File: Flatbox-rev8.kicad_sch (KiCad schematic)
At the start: 72 parts, among them SW1 SW_Push, SW10 GPIO18, SW11 GPIO25, SW12 GPIO27, SW13 GPIO29, SW14 GPIO19, SW15 GPIO24, SW16 GPIO26, SW17 GPIO28, SW18 GPIO16, SW19 SW_Push, SW2 SW_Push, SW20 SW_Push, SW21 GPIO16, SW3 SW_Push, SW4 SW_Push, SW5 SW_Push, SW6 SW_Push, SW7 GPIO9, SW8 GPIO10, SW9 GPIO11, U1 RP2350_60QFN, U2 TLV73333PDBV, U3 W25Q128JVS, Y1 ABM8-272-T3

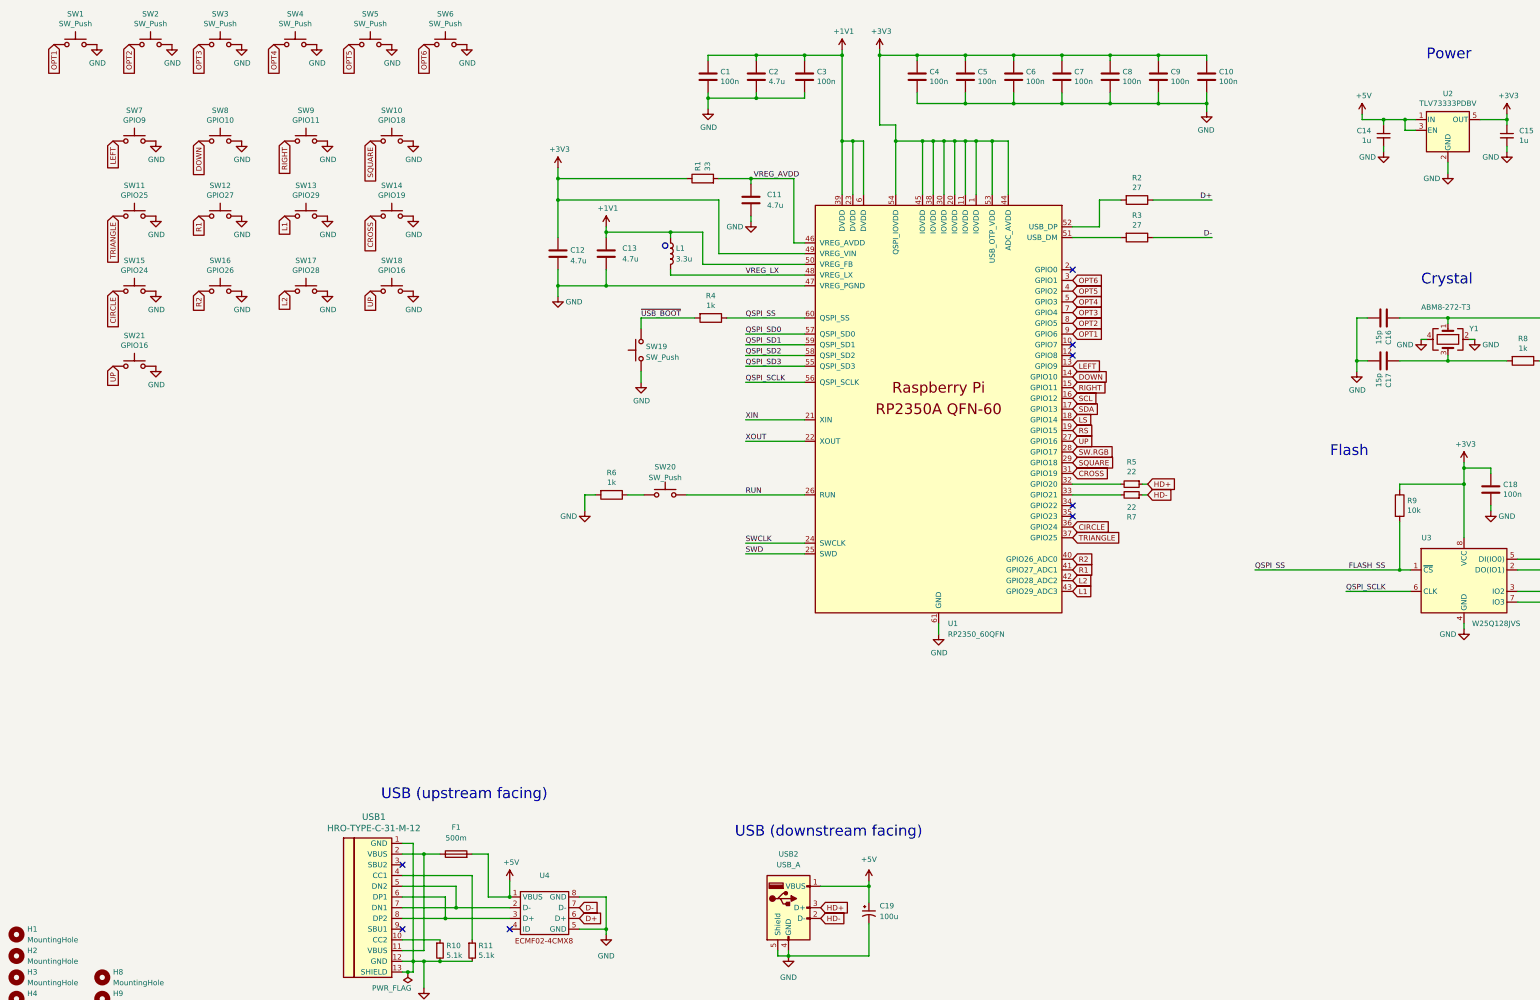
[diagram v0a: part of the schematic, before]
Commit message: Document PHBox design state and sync KiCad sources
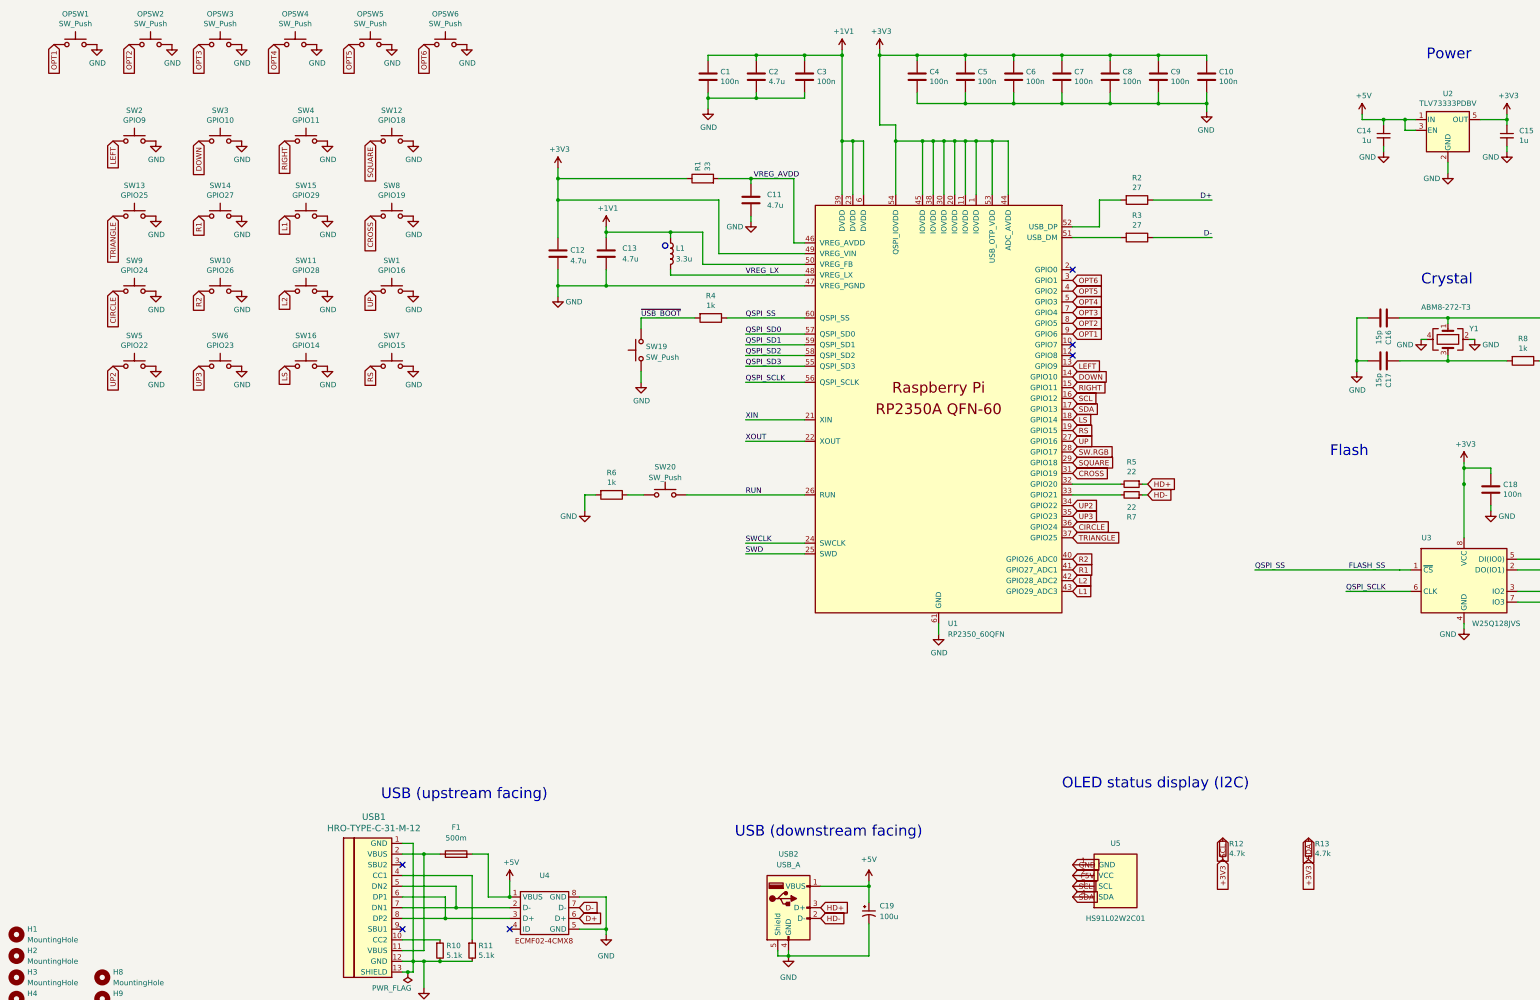
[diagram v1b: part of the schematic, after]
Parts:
- removed R9: 10k, Resistor_SMD:R_0402_1005Metric, symbol Device:R
- added R12, R13: 4.7k, PHBox:R_0603_Compact, symbol Device:R_Small
- added SW16: GPIO14, PCM_Switch_Keyboard_Hotswap_Kailh:SW_Hotswap_Kailh_Choc_V1V2, symbol Switch:SW_Push
- added SW6: GPIO23, PCM_Switch_Keyboard_Hotswap_Kailh:SW_Hotswap_Kailh_Choc_V1V2, symbol Switch:SW_Push
- added SW7: GPIO15, PCM_Switch_Keyboard_Hotswap_Kailh:SW_Hotswap_Kailh_Choc_V1V2, symbol Switch:SW_Push
- added U5: HS91L02W2C01, EasyEDA_Lib:OLED-TH_L38.0-W12.0_HS91L02W2C01, symbol PHBox:HS91L02W2C01_Module
- SW1: renamed from SW18; footprint Kailh:Kailh_socket_PG1350_optional -> PCM_Switch_Keyboard_Hotswap_Kailh:SW_Hotswap_Kailh_Choc_V1V2
- SW10: renamed from SW16; footprint Kailh:Kailh_socket_PG1350_optional -> PCM_Switch_Keyboard_Hotswap_Kailh:SW_Hotswap_Kailh_Choc_V1V2
- SW11: renamed from SW17; footprint Kailh:Kailh_socket_PG1350_optional -> PCM_Switch_Keyboard_Hotswap_Kailh:SW_Hotswap_Kailh_Choc_V1V2
- SW12: renamed from SW10; footprint Kailh:Kailh_socket_PG1350_optional -> PCM_Switch_Keyboard_Hotswap_Kailh:SW_Hotswap_Kailh_Choc_V1V2
- SW13: renamed from SW11; footprint Kailh:Kailh_socket_PG1350_optional -> PCM_Switch_Keyboard_Hotswap_Kailh:SW_Hotswap_Kailh_Choc_V1V2
- SW14: renamed from SW12; footprint Kailh:Kailh_socket_PG1350_optional -> PCM_Switch_Keyboard_Hotswap_Kailh:SW_Hotswap_Kailh_Choc_V1V2
- SW15: renamed from SW13; footprint Kailh:Kailh_socket_PG1350_optional -> PCM_Switch_Keyboard_Hotswap_Kailh:SW_Hotswap_Kailh_Choc_V1V2
- SW2: renamed from SW7; footprint Kailh:Kailh_socket_PG1350_optional -> PCM_Switch_Keyboard_Hotswap_Kailh:SW_Hotswap_Kailh_Choc_V1V2
- SW3: renamed from SW8; footprint Kailh:Kailh_socket_PG1350_optional -> PCM_Switch_Keyboard_Hotswap_Kailh:SW_Hotswap_Kailh_Choc_V1V2
- SW4: renamed from SW9; footprint Kailh:Kailh_socket_PG1350_optional -> PCM_Switch_Keyboard_Hotswap_Kailh:SW_Hotswap_Kailh_Choc_V1V2
- SW5: renamed from SW21; value GPIO16 -> GPIO22; footprint Kailh:Kailh_socket_PG1350_optional -> PCM_Switch_Keyboard_Hotswap_Kailh:SW_Hotswap_Kailh_Choc_V1V2
- SW8: renamed from SW14; footprint Kailh:Kailh_socket_PG1350_optional -> PCM_Switch_Keyboard_Hotswap_Kailh:SW_Hotswap_Kailh_Choc_V1V2
- SW9: renamed from SW15; footprint Kailh:Kailh_socket_PG1350_optional -> PCM_Switch_Keyboard_Hotswap_Kailh:SW_Hotswap_Kailh_Choc_V1V2
- renumbered SW1 to OPSW1, SW2 to OPSW2, SW3 to OPSW3, SW4 to OPSW4, SW5 to OPSW5, SW6 to OPSW6
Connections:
- net +3V3: now also R12.2, R13.2
- net +5V: now also U5.2 (VCC)
- net GND: now also SW16.2, SW6.2, SW7.2, U5.1 (GND)
- net LS: now also SW16.1
- net RS: now also SW7.1
- net SCL: now also R12.1, U5.3 (SCL)
- net SDA: now also R13.1, U5.4 (SDA)
- net UP: no longer SW5.1
- net UP2: now reaches U1.34 (GPIO22)
- net UP2: now also SW5.1
- net UP3: now reaches U1.35 (GPIO23)
- net UP3: now also SW6.1
- no-connect marks 8 -> 6
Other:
- note added: "OLED status display (I2C)"

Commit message: Save validated PHBox design and document testing and manufacturing workflow
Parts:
- added C20, C21, C22, C23, C24, C25, C26, C27, C28, C29, C30, C31, C32, C33, C34, C35, C36, C37, C38, C39, C40: 100n, lib:C_0402_1005Metric_small_pads, symbol Device:C_Small
- added C41: 1u/10V/X7R, Capacitor_SMD:C_0603_1608Metric, symbol Device:C_Small
- added C42, C44: 100n, Capacitor_SMD:C_0402_1005Metric, symbol Device:C_Small
- added C43: 100u/10V, PHBox:CP_KEMET_T520B_3528_21, symbol Device:C_Polarized_Small_US
- added D1, D10, D11, D12, D13, D14, D15, D16, D17, D18, D19, D2, D20, D3, D4, D5, D6, D7, D8, D9: SK6805-EC15, PHBox_Repair:LED_SK6805_EC15_Optical, symbol PHBox:SK6805_EC15_OPSCO
- added D21: ESDA7P120-1U1M, Diode_SMD:ST_QFN-2L_1.6x1.0mm, symbol PHBox:ESDA7P120-1U1M
- added R14: 510R, Resistor_SMD:R_0402_1005Metric, symbol Device:R_Small
- added R15: 200k 1%, Resistor_SMD:R_0402_1005Metric, symbol Device:R_Small
- added R16, R17: 10k, Resistor_SMD:R_0402_1005Metric, symbol Device:R_Small
- added R18, R19, R20, R21, R22, R23, R24, R25, R26, R27, R28, R29, R30, R31, R32, R33: 100R, Resistor_SMD:R_0402_1005Metric, symbol Device:R_Small
- added U6: SN74LV1T34DBVR, SOT-23-5:SOT-23-5, symbol PHBox:SN74LV1T34DBVR
- added U7: TPS2553DBVR, Package_TO_SOT_SMD:SOT-23-6, symbol PHBox:TPS2553DBVR
- added U8: USBLC6-2SC6, Package_TO_SOT_SMD:SOT-23-6, symbol Power_Protection:USBLC6-2SC6
- C19: value 100u -> 100u/10V; footprint Capacitor_Tantalum_SMD:CP_EIA-3528-21_Kemet-B -> PHBox:CP_KEMET_T520B_3528_21; LCSC C16133 -> C600583; MPN (none) -> T520B107M010ATE070; Manufacturer (none) -> KEMET
- F1: value 500m -> 750mA hold; symbol Device:Fuse -> Device:Polyfuse; LCSC C2833485 -> C19108399; MPN (none) -> SMD0805-075-12V; Manufacturer (none) -> TECHFUSE
- SW1, SW10, SW11, SW12, SW13, SW14, SW15, SW16, SW2, SW3, SW4, SW5, SW6, SW7, SW8, SW9: footprint PCM_Switch_Keyboard_Hotswap_Kailh:SW_Hotswap_Kailh_Choc_V1V2 -> PHBox_Repair:SW_Hotswap_Kailh_Choc_V1V2_3D_Optical
- SW19, SW20: footprint SW:C318884 -> PHBox_Repair:SW_C318884_FabOnly
- U3: symbol Memory_Flash:W25Q128JVS -> PHBox:Layout_Memory_Flash_W25Q128JVS
- U4: value ~ -> ECMF2-40A100N6; footprint ECMF02-4CMX8:ECMF02-4CMX8 -> PHBox:ECMF2-40A100N6; symbol ECMF02-4CMX8:ECMF02-4CMX8 -> PHBox:ECMF2-40A100N6; LCSC C717678 -> C5267592; MPN (none) -> ECMF2-40A100N6; Manufacturer (none) -> STMicroelectronics
- U5: value HS91L02W2C01 -> WEA012864DWPP3N00003; footprint EasyEDA_Lib:OLED-TH_L38.0-W12.0_HS91L02W2C01 -> PHBox:OLED_WEA012864DWPP3N00003; symbol PHBox:HS91L02W2C01_Module -> PHBox:WEA012864DWPP3N00003; LCSC C5248081 -> (none); MPN HS91L02W2C01 -> WEA012864DWPP3N00003; Manufacturer HS -> Winstar
- USB2: symbol Connector:USB_A -> PHBox:Layout_Connector_USB_A
- Y1: symbol Device:Crystal_GND24 -> PHBox:Layout_Device_Crystal_GND24
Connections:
- net +3V3: now also U5.1 (VCC), C41.1, R17.1
- net +5V: now also C20.1, C21.1, C22.1, C23.1, C24.1, C25.1, C26.1, C27.1, C28.1, C29.1, C30.1, C31.1, C32.1, C33.1, C34.1, C35.1, C36.1, C37.1, C38.1, C39.1, C40.1, C42.1, D1.2 (VDD), D10.2 (VDD), D11.2 (VDD), D12.2 (VDD), D13.2 (VDD), D14.2 (VDD), D15.2 (VDD), D16.2 (VDD), D17.2 (VDD), D18.2 (VDD), D19.2 (VDD), D2.2 (VDD), D20.2 (VDD), D3.2 (VDD), D4.2 (VDD), D5.2 (VDD), D6.2 (VDD), D7.2 (VDD), D8.2 (VDD), D9.2 (VDD), U6.5 (VCC), U7.1 (IN); no longer C19.1, U4.1 (VBUS), U5.2 (VCC), USB2.1 (VBUS)
- net D-: now also U4.5 (D- to IC); no longer U4.7 (D-)
- net GND: now also U4.3 (GND), U4.4 (GND), U5.2 (GND), C20.2, C21.2, C22.2, C23.2, C24.2, C25.2, C26.2, C27.2, C28.2, C29.2, C30.2, C31.2, C32.2, C33.2, C34.2, C35.2, C36.2, C37.2, C38.2, C39.2, C40.2, C41.2, C42.2, C43.2, C44.2, D1.4 (GND), D10.4 (GND), D11.4 (GND), D12.4 (GND), D13.4 (GND), D14.4 (GND), D15.4 (GND), D16.4 (GND), D17.4 (GND), D18.4 (GND), D19.4 (GND), D2.4 (GND), D20.4 (GND), D21.2 (A), D3.4 (GND), D4.4 (GND), D5.4 (GND), D6.4 (GND), D7.4 (GND), D8.4 (GND), D9.4 (GND), R15.2, R16.1, U6.3 (GND), U7.2 (GND), U8.2 (GND); no longer U4.5 (GND), U4.8 (GND), U5.1 (GND)
- net HD+: now also U8.1 (I/O1), U8.6 (I/O1)
- net HD-: now also U8.3 (I/O2), U8.4 (I/O2)
- net SCL: now also U1.17 (GPIO13); no longer U1.16 (GPIO12)
- net SDA: now also U1.16 (GPIO12); no longer U1.17 (GPIO13)
- net at F1.1, USB1.11 (VBUS), USB1.2 (VBUS): now also D21.1 (K)
- net at USB1.6 (DP1), USB1.8 (DP2): now also U4.1 (D+ to connector); no longer U4.3 (D+)
- net USB_HOST_EN: now reaches U1.10 (GPIO7)
- net USB_HOST_EN: now also R16.2, U7.3 (EN)
- net RGB: now reaches U1.12 (GPIO8)
- net RGB: now also U6.2 (A)
- net FLASH_SS renamed QSPI_SS
- net SW.RGB renamed USB_HOST_FAULT_N
- net USB_HOST_FAULT_N: now also R17.2, U7.4 (FAULT_N)
- net SWCLK: no longer names the net of U1.24 (SWCLK)
- net SWD: no longer names the net of U1.25 (SWD)
- new net: D15.3 (DOUT), R32.1
- new net: D16.1 (DIN), R32.2
- new net: D11.3 (DOUT), R28.1
- new net: D12.1 (DIN), R28.2
- new net: D10.3 (DOUT), R27.1
- new net: D16.3 (DOUT), R33.1
- new net: D17.1 (DIN), R33.2
- new net: D1.3 (DOUT), R18.1
- new net: D2.1 (DIN), R18.2
- new net: D4.3 (DOUT), R21.1
- new net: D5.1 (DIN), R21.2
- new net: D2.3 (DOUT), R19.1
- new net: D3.1 (DIN), R19.2
- new net: D8.3 (DOUT), R25.1
- new net: D9.1 (DIN), R25.2
- new net: D3.3 (DOUT), R20.1
- new net: D4.1 (DIN), R20.2
- new net: D13.3 (DOUT), R30.1
- new net: D14.1 (DIN), R30.2
- new net: D9.3 (DOUT), R26.1
- new net: D10.1 (DIN), R26.2
- new net: D12.3 (DOUT), R29.1
- new net: D13.1 (DIN), R29.2
- new net: D6.3 (DOUT), R23.1
- new net: D7.1 (DIN), R23.2
- new net: D7.3 (DOUT), R24.1
- new net: D8.1 (DIN), R24.2
- new net: D14.3 (DOUT), R31.1
- new net: D15.1 (DIN), R31.2
- new net: D5.3 (DOUT), R22.1
- new net: D6.1 (DIN), R22.2
- new net: D17.3 (DOUT), D18.1 (DIN)
- new net: D18.3 (DOUT), D19.1 (DIN)
- new net: D19.3 (DOUT), D20.1 (DIN)
- new net LED_BUFFER_Y: R14.1, U6.4 (Y)
- new net LED_DATA_IN: D1.1 (DIN), R14.2
- new net LED_HOP_10: D11.1 (DIN), R27.2
- new net USB_HOST_5V: C19.1, C43.1, C44.1, U7.6 (OUT), U8.5 (VBUS), USB2.1 (VBUS)
- new net USB_HOST_ILIM: R15.1, U7.5 (ILIM)
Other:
- note added: "EDGE 1 / index 16"
- note added: "EDGE 2 / index 17"
- note added: "EDGE 3 / index 18"
- note added: "EDGE 4 / index 19"
- note added: "GP2040-CE Max Brightness target: 127/255 (~50%). Firmware setting; not a current limiter."
- note added: "RGB source: GPIO8. Verify 13-button off indices 5, 6, 15 in firmware."
- note added: "SW1 / index 0"
- note added: "SW10 / index 9"
- note added: "SW11 / index 10"
- note added: "SW12 / index 11"
- note added: "SW13 / index 12"
- note added: "SW14 / index 13"
- note added: "SW15 / index 14"
- note added: "SW16 / index 15"
- note added: "SW2 / index 1"
- note added: "SW3 / index 2"
- note added: "SW4 / index 3"
- note added: "SW5 / index 4"
- note added: "SW6 / index 5"
- note added: "SW7 / index 6"
- note added: "SW8 / index 7"
- note added: "SW9 / index 8"
- note added: "USB2 dongle-only VBUS: 200k ILIM = 135mA nominal (115-159mA incl. 1% R); not a total USB input limit"
- moved on the sheet: R4, SW19
